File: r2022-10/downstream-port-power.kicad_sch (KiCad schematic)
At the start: 33 parts, among them J4 USB_A (female down), J5 USB_A_Stacked, J6 USB_A_Stacked, J7 USB_A_Stacked, U10 APL3511C, U11 NUP4202, U12 NUP4202, U13 NUP4202, U14 NUP4202, U15 NUP4202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

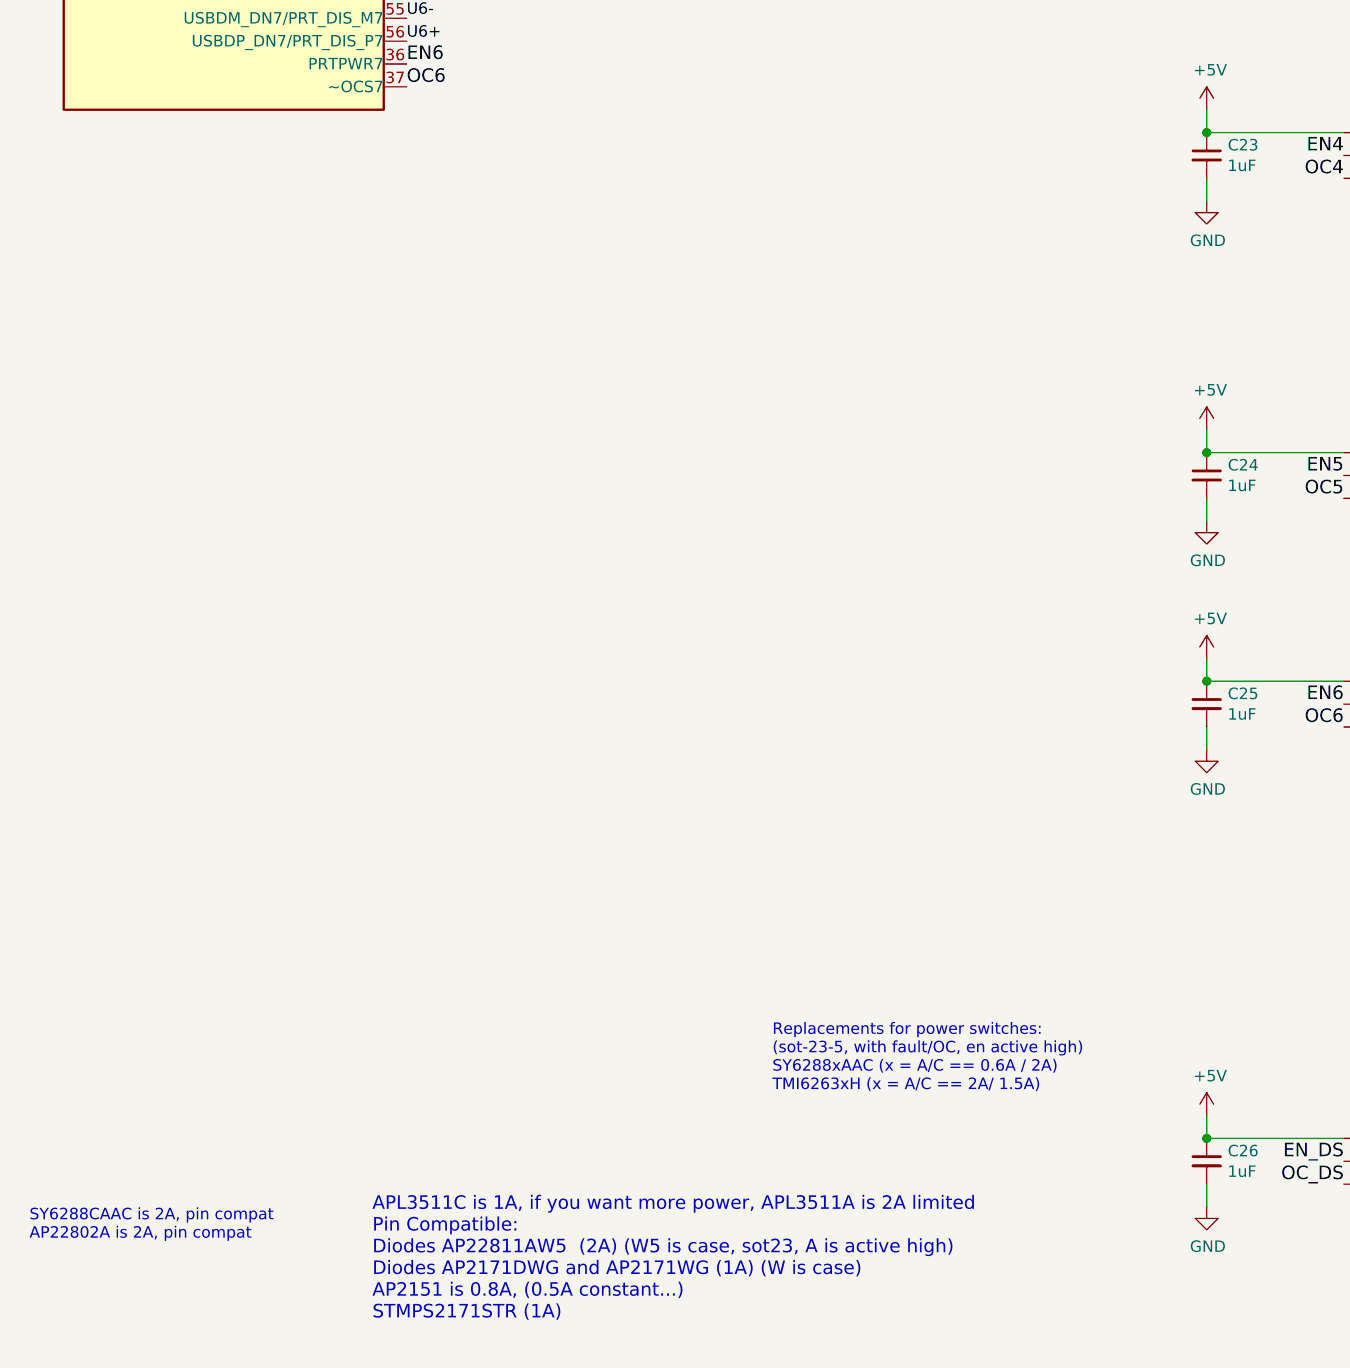
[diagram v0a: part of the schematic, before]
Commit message: rev3: overhaul nearly all parts to be from jlc pcba
Only the inductor left.  I've marked a few through hole parts as DNP, as
I can solder them by hand, and already have the parts in stock.  But
everything else goes to JLC for assembly, with every attempt made to
stick to only basic parts, or shared parts.  Beyond that, price and
stocking!
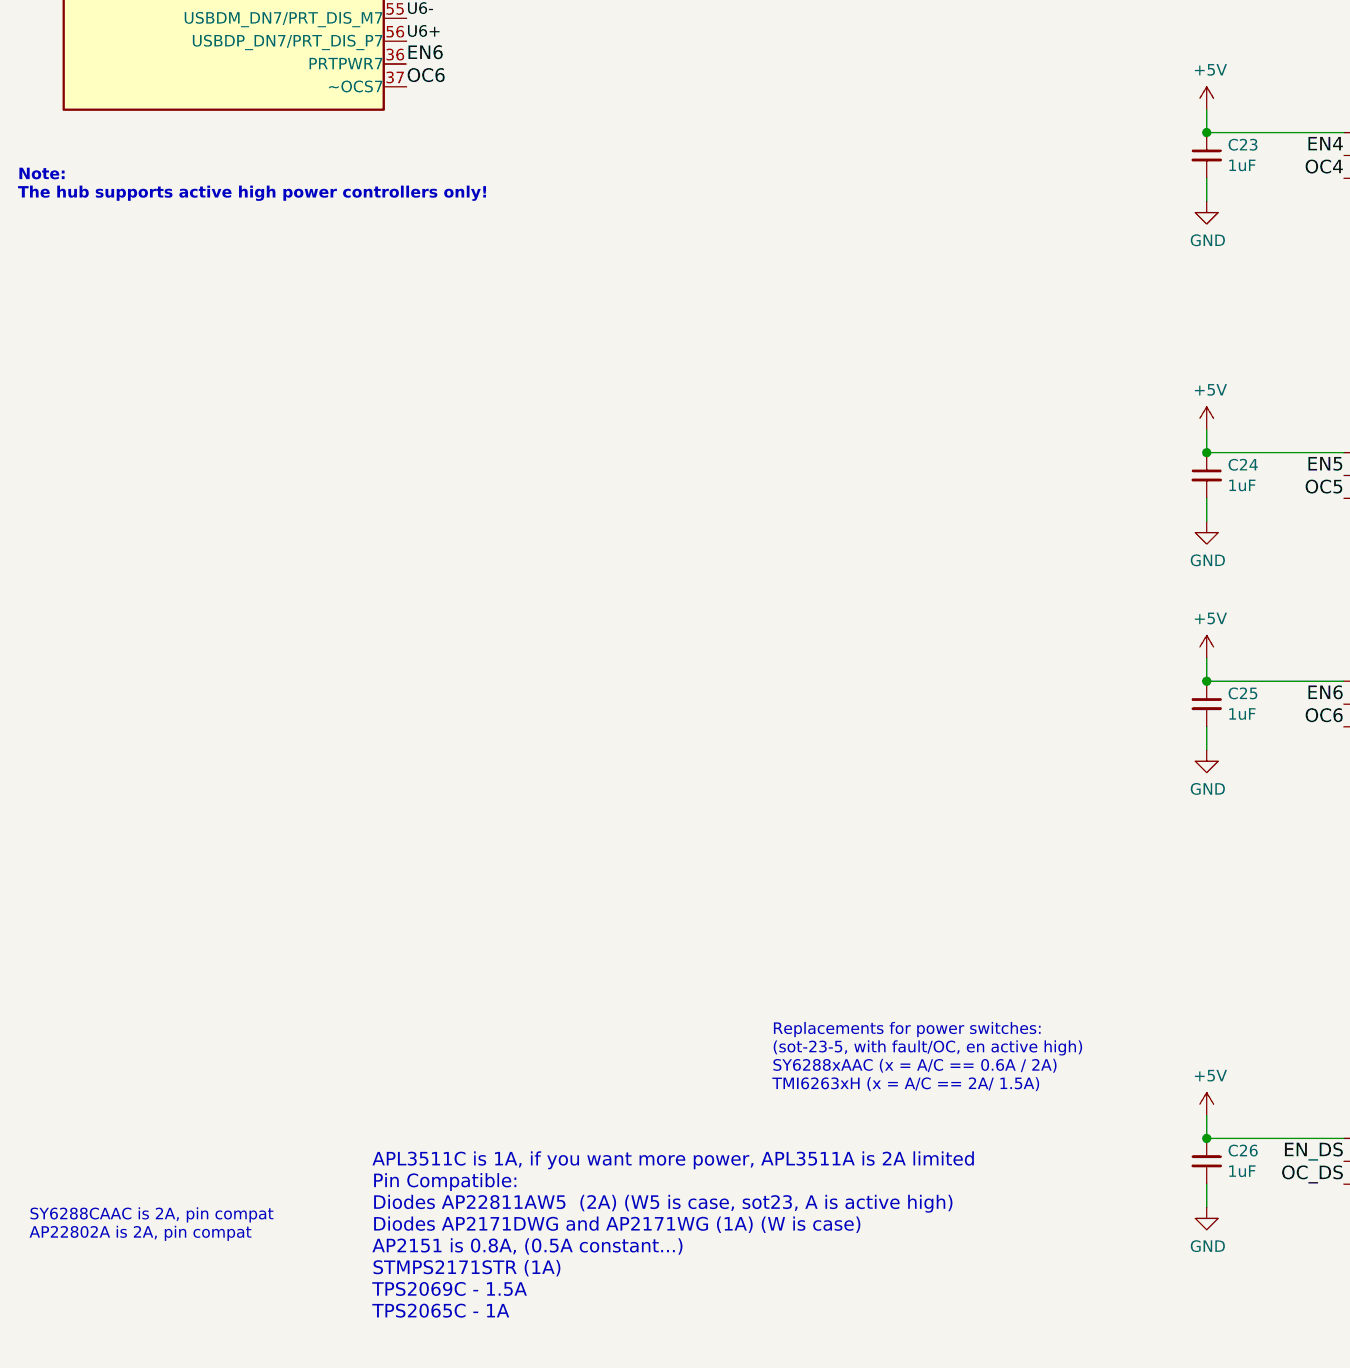
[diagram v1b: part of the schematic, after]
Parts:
- J4: DNP (none) -> 1; MPN C42643 or SS-52100 compatible -> 902-141A1011D10100; jlc-basic (none) -> 0; lcsc# (none) -> C42643
- J5, J6, J7: DNP (none) -> 1; MPN (none) -> 907-111A1012D10200; jlc-basic (none) -> 0; lcsc# (none) -> C2341
- U10, U4, U5, U6, U7, U8, U9: MPN (none) -> AP22802AW5-7; jlc-basic (none) -> 0; lcsc# (none) -> C211404
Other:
- note added: "APL3511C is 1A, if you want more power, APL3511A is 2A limited Pin Compatible: Diodes AP22811AW5 (2A) (W5 is case, sot23, A is active high) Diodes AP2171DWG and AP2171WG (1A) (W is case) AP2151 is 0.8A, (0.5A constant...) STMPS2171STR (1A) TPS2069C - 1.5A TPS2065C - 1A"
- note added: "Note: The hub supports active high power controllers only!"
- note removed: "APL3511C is 1A, if you want more power, APL3511A is 2A limited Pin Compatible: Diodes AP22811AW5 (2A) (W5 is case, sot23, A is active high) Diodes AP2171DWG and AP2171WG (1A) (W is case) AP2151 is 0.8A, (0.5A constant...) STMPS2171STR (1A)"
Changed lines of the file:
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@@
     (stroke (width 0) (type solid) (color 0 0 0 0))
+  )
+  (text "Note:\nThe hub supports active high power controllers only!"
+    (at 45.72 149.86 0)
+    (effects (font (size 1.27 1.27) (thickness 0.254) bold) (justify left bottom))
   )
   (text "Downstream port for cascading to another hub\nPower switching as well, because why not!"
@@
     (effects (font (size 1.27 1.27)) (justify left bottom))
   )
-  (text "APL3511C is 1A, if you want more power, APL3511A is 2A limited\nPin Compatible:\nDiodes AP22811AW5  (2A) (W5 is case, sot23, A is active high)\nDiodes AP2171DWG and AP2171WG (1A) (W is case)\nAP2151 is 0.8A, (0.5A constant...)\nSTMPS2171STR (1A)\n"
+  (text "APL3511C is 1A, if you want more power, APL3511A is 2A limited\nPin Compatible:\nDiodes AP22811AW5  (2A) (W5 is case, sot23, A is active high)\nDiodes AP2171DWG and AP2171WG (1A) (W is case)\nAP2151 is 0.8A, (0.5A constant...)\nSTMPS2171STR (1A)\nTPS2069C - 1.5A\nTPS2065C - 1A\n"
     (at 85.09 274.32 0)
     (effects (font (size 1.4986 1.4986)) (justify left bottom))
@@
       (effects (font (size 1.27 1.27)) hide)
     )
-    (property "MPN" "C42643 or SS-52100 compatible" (id 4) (at 264.16 259.08 0)
+    (property "MPN" "902-141A1011D10100" (id 4) (at 264.16 259.08 0)
+      (effects (font (size 1.27 1.27)) hide)
+    )
+    (property "DNP" "1" (id 5) (at 264.16 259.08 0)
+      (effects (font (size 1.27 1.27)) hide)
+    )
+    (property "jlc-basic" "0" (id 6) (at 264.16 259.08 0)
+      (effects (font (size 1.27 1.27)) hide)
+    )
+    (property "lcsc#" "C42643" (id 7) (at 264.16 259.08 0)
       (effects (font (size 1.27 1.27)) hide)
     )
@@
       (effects (font (size 1.27 1.27)) hide)
     )
+    (property "MPN" "AP22802AW5-7" (id 4) (at 200.66 180.34 0)
+      (effects (font (size 1.27 1.27)) hide)
+    )
+    (property "jlc-basic" "0" (id 5) (at 200.66 180.34 0)
+      (effects (font (size 1.27 1.27)) hide)
+    )
+    (property "lcsc#" "C211404" (id 6) (at 200.66 180.34 0)
+      (effects (font (size 1.27 1.27)) hide)
+    )
     (pin "1")
     (pin "2")
@@
       (effects (font (size 1.27 1.27)) hide)
     )
+    (property "MPN" "AP22802AW5-7" (id 4) (at 200.66 205.74 0)
+      (effects (font (size 1.27 1.27)) hide)
+    )
+    (property "jlc-basic" "0" (id 5) (at 200.66 205.74 0)
+      (effects (font (size 1.27 1.27)) hide)
+    )
+    (property "lcsc#" "C211404" (id 6) (at 200.66 205.74 0)
+      (effects (font (size 1.27 1.27)) hide)
+    )
     (pin "1")
     (pin "2")
@@
     )
     (property "Datasheet" "http://www.anpec.com.tw/ashx_prod_file.ashx?prod_id=458&file_path=20180420152940150.pdf&original_name=APL3511A.pdf" (id 3) (at 205.74 157.48 0)
+      (effects (font (size 1.27 1.27)) hide)
+    )
+    (property "MPN" "AP22802AW5-7" (id 4) (at 200.66 144.78 0)
+      (effects (font (size 1.27 1.27)) hide)
+    )
+    (property "jlc-basic" "0" (id 5) (at 200.66 144.78 0)
+      (effects (font (size 1.27 1.27)) hide)
+    )
+    (property "lcsc#" "C211404" (id 6) (at 200.66 144.78 0)
       (effects (font (size 1.27 1.27)) hide)
     )
@@
       (effects (font (size 1.27 1.27)) hide)
     )
+    (property "MPN" "AP22802AW5-7" (id 4) (at 200.66 40.64 0)
+      (effects (font (size 1.27 1.27)) hide)
+    )
+    (property "jlc-basic" "0" (id 5) (at 200.66 40.64 0)
+      (effects (font (size 1.27 1.27)) hide)
+    )
+    (property "lcsc#" "C211404" (id 6) (at 200.66 40.64 0)
+      (effects (font (size 1.27 1.27)) hide)
+    )
     (pin "1")
     (pin "2")
@@
       (effects (font (size 1.27 1.27)) hide)
     )
+    (property "MPN" "AP22802AW5-7" (id 4) (at 200.66 68.58 0)
+      (effects (font (size 1.27 1.27)) hide)
+    )
+    (property "jlc-basic" "0" (id 5) (at 200.66 68.58 0)
+      (effects (font (size 1.27 1.27)) hide)
+    )
+    (property "lcsc#" "C211404" (id 6) (at 200.66 68.58 0)
+      (effects (font (size 1.27 1.27)) hide)
+    )
     (pin "1")
     (pin "2")
@@
     )
     (property "Datasheet" "http://www.anpec.com.tw/ashx_prod_file.ashx?prod_id=458&file_path=20180420152940150.pdf&original_name=APL3511A.pdf" (id 3) (at 205.74 129.54 0)
+      (effects (font (size 1.27 1.27)) hide)
+    )
+    (property "MPN" "AP22802AW5-7" (id 4) (at 200.66 116.84 0)
+      (effects (font (size 1.27 1.27)) hide)
+    )
+    (property "jlc-basic" "0" (id 5) (at 200.66 116.84 0)
+      (effects (font (size 1.27 1.27)) hide)
+    )
+    (property "lcsc#" "C211404" (id 6) (at 200.66 116.84 0)
       (effects (font (size 1.27 1.27)) hide)
     )
@@
     )
     (property "Datasheet" " ~" (id 3) (at 297.18 123.19 0)
+      (effects (font (size 1.27 1.27)) hide)
+    )
+    (property "MPN" "907-111A1012D10200" (id 4) (at 302.26 124.46 0)
+      (effects (font (size 1.27 1.27)) hide)
+    )
+    (property "jlc-basic" "0" (id 5) (at 302.26 124.46 0)
+      (effects (font (size 1.27 1.27)) hide)
+    )
+    (property "lcsc#" "C2341" (id 6) (at 302.26 124.46 0)
+      (effects (font (size 1.27 1.27)) hide)
+    )
+    (property "DNP" "1" (id 7) (at 302.26 124.46 0)
       (effects (font (size 1.27 1.27)) hide)
     )
@@
       (effects (font (size 1.27 1.27)) hide)
     )
+    (property "MPN" "907-111A1012D10200" (id 4) (at 302.26 48.26 0)
+      (effects (font (size 1.27 1.27)) hide)
+    )
+    (property "jlc-basic" "0" (id 5) (at 302.26 48.26 0)
+      (effects (font (size 1.27 1.27)) hide)
+    )
+    (property "lcsc#" "C2341" (id 6) (at 302.26 48.26 0)
+      (effects (font (size 1.27 1.27)) hide)
+    )
+    (property "DNP" "1" (id 7) (at 302.26 48.26 0)
+      (effects (font (size 1.27 1.27)) hide)
+    )
     (pin "1")
     (pin "2")
@@
       (effects (font (size 1.27 1.27)) hide)
     )
+    (property "MPN" "AP22802AW5-7" (id 4) (at 200.66 256.54 0)
+      (effects (font (size 1.27 1.27)) hide)
+    )
+    (property "jlc-basic" "0" (id 5) (at 200.66 256.54 0)
+      (effects (font (size 1.27 1.27)) hide)
+    )
+    (property "lcsc#" "C211404" (id 6) (at 200.66 256.54 0)
+      (effects (font (size 1.27 1.27)) hide)
+    )
     (pin "1")
     (pin "2")
@@
       (effects (font (size 1.27 1.27)) hide)
     )
+    (property "MPN" "907-111A1012D10200" (id 4) (at 302.26 187.96 0)
+      (effects (font (size 1.27 1.27)) hide)
+    )
+    (property "jlc-basic" "0" (id 5) (at 302.26 187.96 0)
+      (effects (font (size 1.27 1.27)) hide)
+    )
+    (property "lcsc#" "C2341" (id 6) (at 302.26 187.96 0)
+      (effects (font (size 1.27 1.27)) hide)
+    )
+    (property "DNP" "1" (id 7) (at 302.26 187.96 0)
+      (effects (font (size 1.27 1.27)) hide)
+    )
